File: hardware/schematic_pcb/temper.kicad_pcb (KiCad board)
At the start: 2 copper layers, 36 x 96.5 mm, 60 parts, among them J1 conn_01x03, J2 conn_01x03, J3 conn_01x03, J4 conn_01x03, J5 Charge Connector, J6 MCU Serial I/F, J7 Conn_01x10, M1 AO3401A, Q1 2N7002, Q2 2N7002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

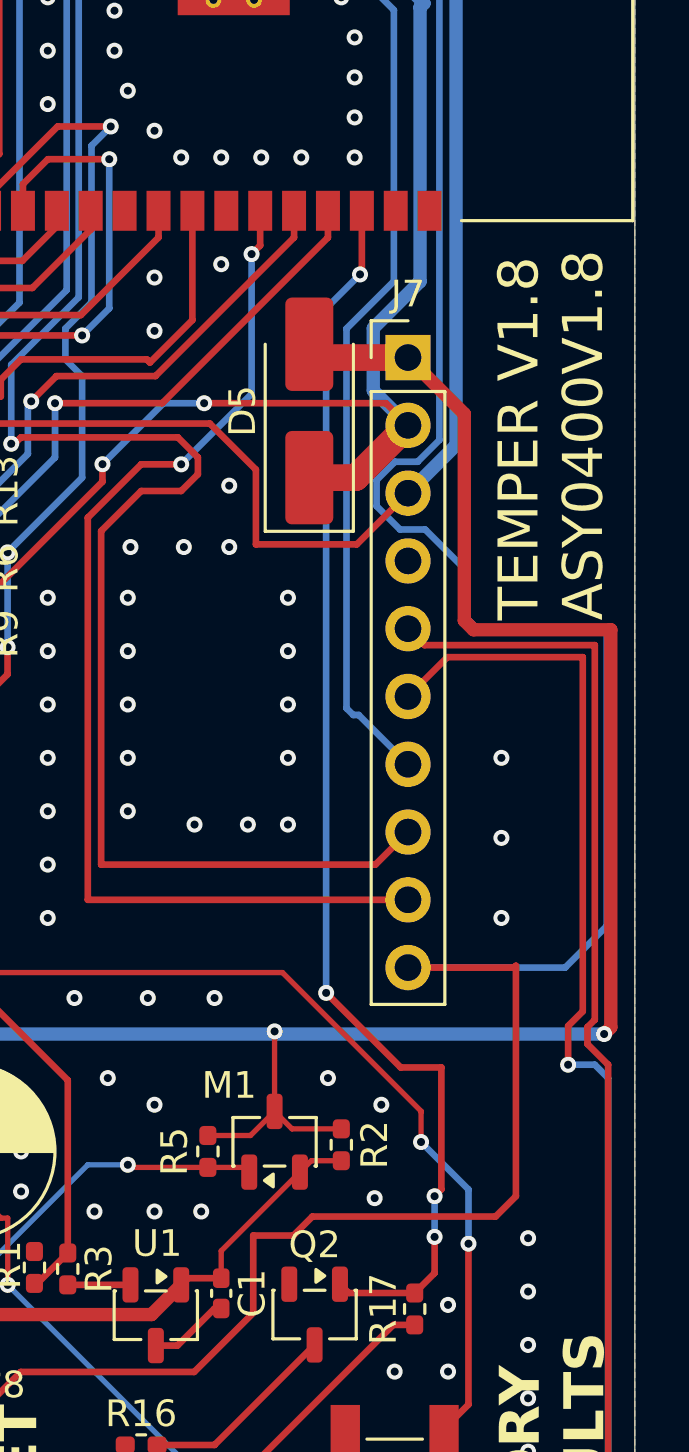
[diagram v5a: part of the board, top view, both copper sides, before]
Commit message: - Fix incorrect M1 connectivity. - Bump PCB to V2.0
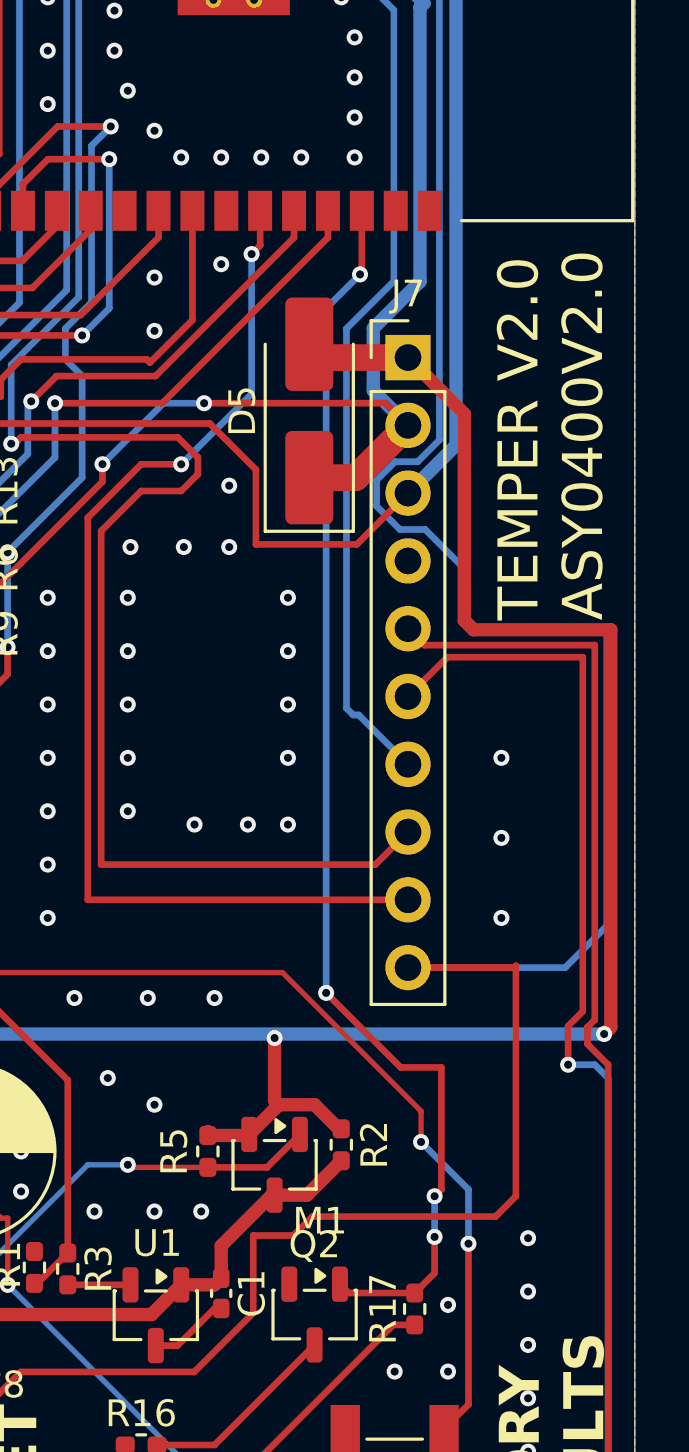
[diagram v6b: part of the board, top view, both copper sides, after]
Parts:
- moved M1 0.86 mm to (152.5, 121.2), turned to -90 degrees
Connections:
- M1 pad 2: Net-(J1-Pin_3) -> +5v
- M1 pad 3: +5v -> Net-(J1-Pin_3)
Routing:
- net Net-(M1-G1): track 109.1 -> 111.4 mm
- net GND: vias 114 -> 111
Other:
- board text added: "TEMPER V2.0 ASY0400V2.0"
- board text removed: "TEMPER V1.8 ASY0400V1.8"
